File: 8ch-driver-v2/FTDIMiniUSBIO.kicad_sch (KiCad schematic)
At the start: 5 parts, among them J5 CN2, J6 CN3, U18 BD33FC0FP

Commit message: progress
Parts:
- removed J5: CN2, symbol Connector_Generic:Conn_02x13_Odd_Even
- removed J6: CN3, symbol Connector_Generic:Conn_02x13_Odd_Even
- added U17: FT4232H MINI MODULE, FT4232H_FTD, symbol 2024-07-09_22-42-21:FT4232H_MINI_MODULE
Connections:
- net +3.3V: now also U17.CN2-1 (V3V3), U17.CN2-3 (V3V3), U17.CN2-5 (V3V3)
- net GND: now also U17.CN2-2 (GND), U17.CN2-4 (GND), U17.CN2-6 (GND)
- net Relay01: now also U17.CN2-7 (AD0)
- net Relay02: now also U17.CN2-10 (AD1)
- net Relay03: now also U17.CN2-9 (AD2)
- net Relay04: now also U17.CN2-12 (AD3)
- net Relay05: now also U17.CN2-14 (AD4)
- net Relay06: now also U17.CN2-13 (AD5)
- net Relay07: now also U17.CN2-16 (AD6)
- net Relay08: now also U17.CN2-15 (AD7)
- net Relay09: now also U17.CN3-26 (CD0)
- net Relay10: now also U17.CN3-25 (CD1)
- net Relay11: now also U17.CN3-24 (CD2)
- net Relay12: now also U17.CN3-23 (CD3)
- net Relay13: now also U17.CN3-21 (CD4)
- net Relay14: now also U17.CN3-20 (CD5)
- net Relay15: now also U17.CN3-19 (CD6)
- net Relay16: now also U17.CN3-18 (CD7)
- new net: U17.CN3-1 (VBUS), U17.CN3-3 (VCC)

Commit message: mucho mas progresso
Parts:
- renumbered C53 to C50, C54 to C51, U18 to U17, U17 to U18
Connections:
- net Relay01 renamed USBTTLOut01
- net Relay02 renamed USBTTLOut02
- net Relay03 renamed USBTTLOut03
- net Relay04 renamed USBTTLOut04
- net Relay05 renamed USBTTLOut05
- net Relay06 renamed USBTTLOut06
- net Relay07 renamed USBTTLOut07
- net Relay08 renamed USBTTLOut08
- net Relay09 renamed USBTTLOut09
- net Relay10 renamed USBTTLOut10
- net Relay11 renamed USBTTLOut11
- net Relay12 renamed USBTTLOut12
- net Relay13 renamed USBTTLOut13
- net Relay14 renamed USBTTLOut14
- net Relay15 renamed USBTTLOut15
- net Relay16 renamed USBTTLOut16

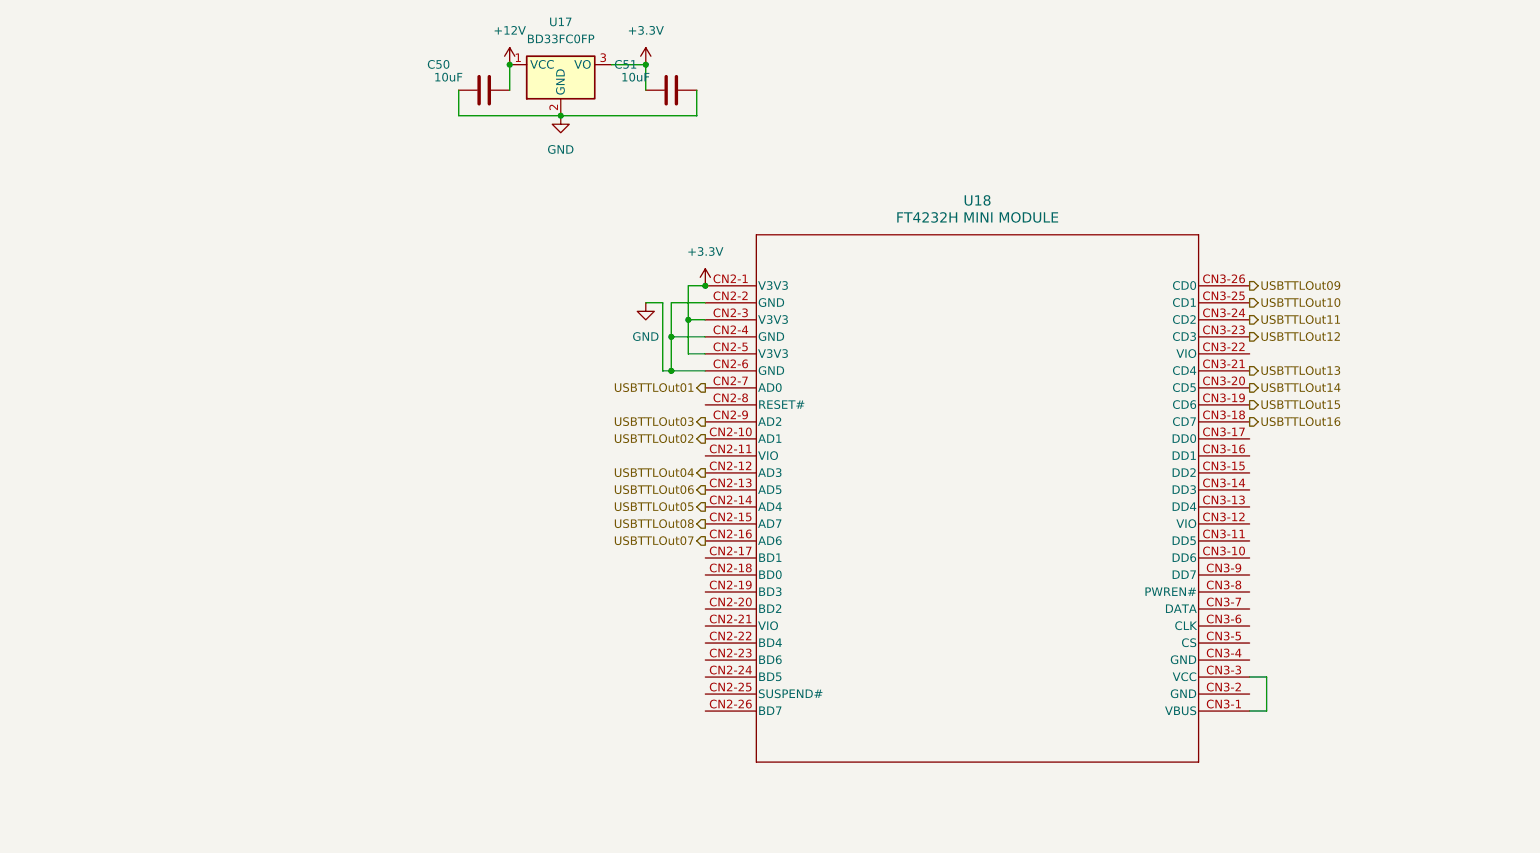
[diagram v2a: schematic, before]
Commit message: 16-valve PCB layout for inspection
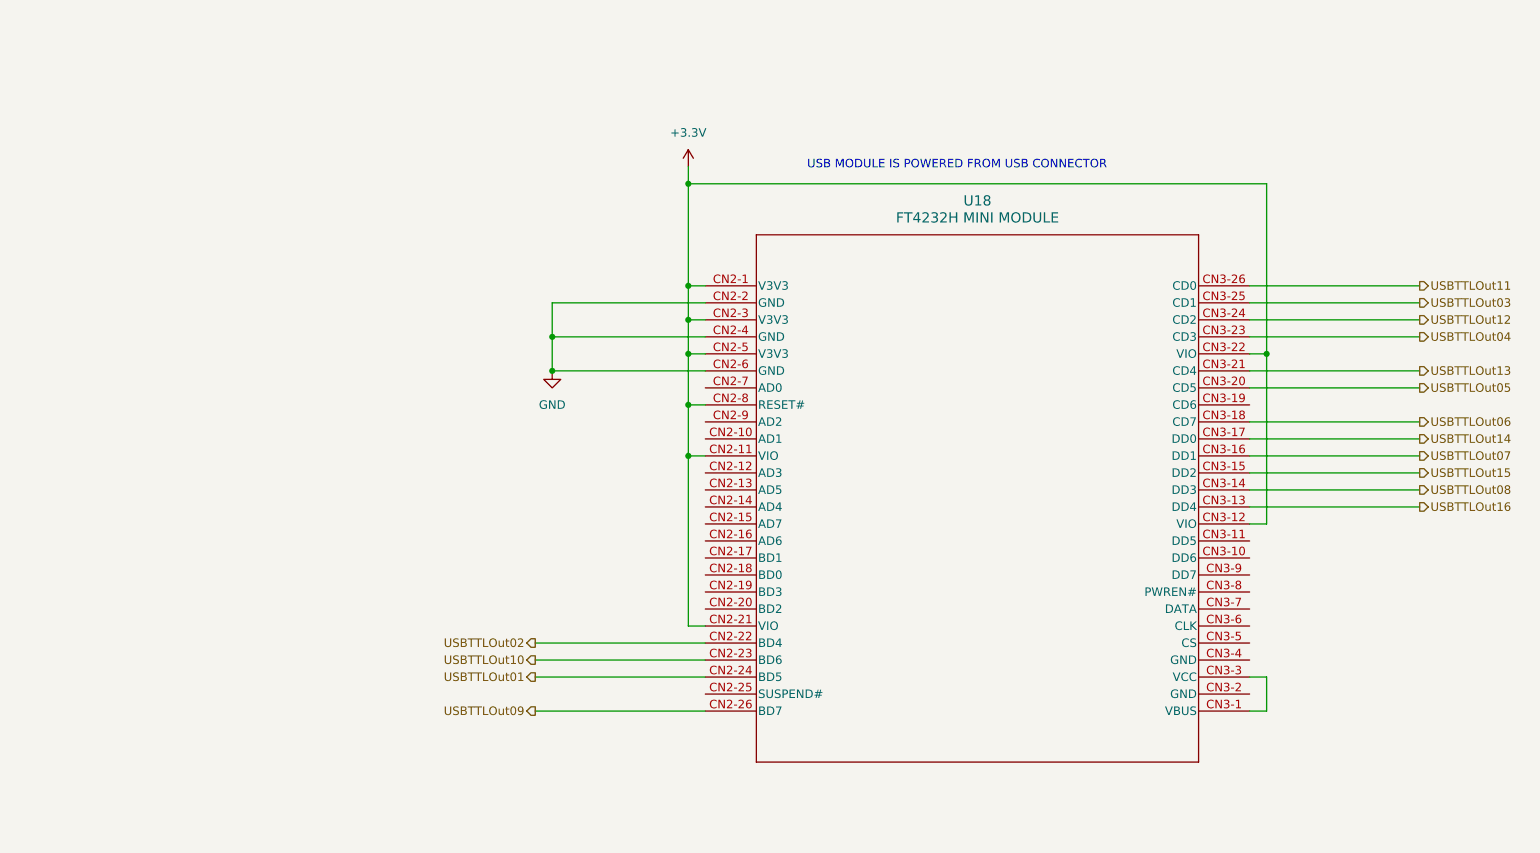
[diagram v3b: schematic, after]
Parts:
- removed C50, C51: 10uF, Capacitor_SMD:C_1210_3225Metric, symbol Device:C
- removed U17: BD33FC0FP, Package_TO_SOT_SMD:TO-252-2, symbol Regulator_Linear:BD33FC0FP
- U18: footprint FT4232H_FTD -> footprint:FT4232H_MINI_MODULE
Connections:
- net +3.3V: now also U18.CN2-11 (VIO), U18.CN2-21 (VIO), U18.CN2-8 (RESET#), U18.CN3-12 (VIO), U18.CN3-22 (VIO)
- net USBTTLOut01: now also U18.CN2-24 (BD5); no longer U18.CN2-7 (AD0)
- net USBTTLOut02: now also U18.CN2-22 (BD4); no longer U18.CN2-10 (AD1)
- net USBTTLOut03: now also U18.CN3-25 (CD1); no longer U18.CN2-9 (AD2)
- net USBTTLOut04: now also U18.CN3-23 (CD3); no longer U18.CN2-12 (AD3)
- net USBTTLOut05: now also U18.CN3-20 (CD5); no longer U18.CN2-14 (AD4)
- net USBTTLOut06: now also U18.CN3-18 (CD7); no longer U18.CN2-13 (AD5)
- net USBTTLOut07: now also U18.CN3-16 (DD1); no longer U18.CN2-16 (AD6)
- net USBTTLOut08: now also U18.CN3-14 (DD3); no longer U18.CN2-15 (AD7)
- net USBTTLOut09: now also U18.CN2-26 (BD7); no longer U18.CN3-26 (CD0)
- net USBTTLOut10: now also U18.CN2-23 (BD6); no longer U18.CN3-25 (CD1)
- net USBTTLOut11: now also U18.CN3-26 (CD0); no longer U18.CN3-24 (CD2)
- net USBTTLOut12: now also U18.CN3-24 (CD2); no longer U18.CN3-23 (CD3)
- net USBTTLOut14: now also U18.CN3-17 (DD0); no longer U18.CN3-20 (CD5)
- net USBTTLOut15: now also U18.CN3-15 (DD2); no longer U18.CN3-19 (CD6)
- net USBTTLOut16: now also U18.CN3-13 (DD4); no longer U18.CN3-18 (CD7)
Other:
- note added: "USB MODULE IS POWERED FROM USB CONNECTOR"
